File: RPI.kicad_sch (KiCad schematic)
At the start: 29 parts, among them J1 Conn_01x02_Male, J2 GPIO, J5 Conn_01x06, J6 Conn_01x04, J7 Conn_01x03, J8 Conn_01x02, J9 Conn_01x02, Q1 IRF9540N, Q2 IRF9540N, Q3 BC856BDW1, SW1 SW_SPDT, SW2 SW_SPDT, U1 LM1085-ADJ

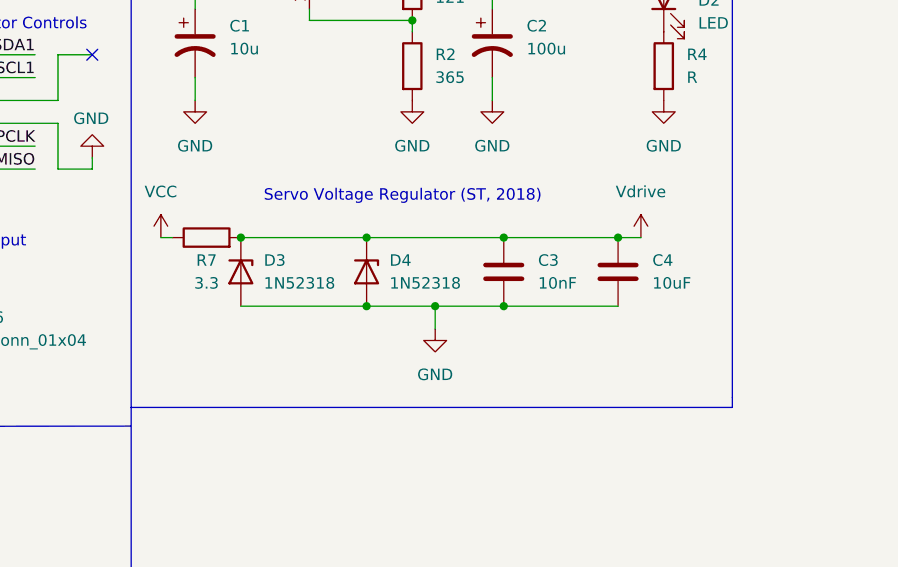
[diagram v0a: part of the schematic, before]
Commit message: Further updated with more resistors
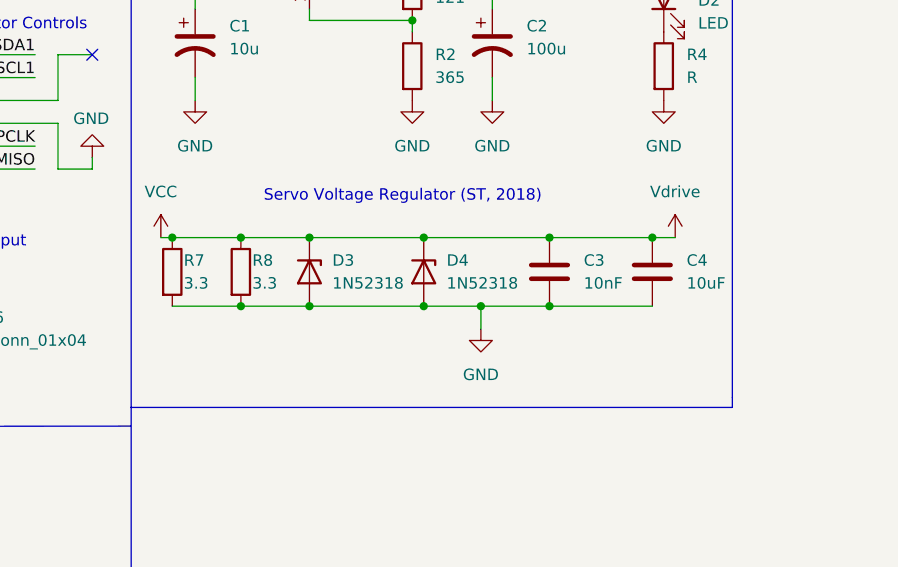
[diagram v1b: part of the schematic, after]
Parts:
- added R8: 3.3, Resistor_SMD:R_0805_2012Metric_Pad1.20x1.40mm_HandSolder, symbol Device:R
- R7: footprint Resistor_THT:R_Axial_DIN0207_L6.3mm_D2.5mm_P10.16mm_Horizontal -> Resistor_SMD:R_0805_2012Metric_Pad1.20x1.40mm_HandSolder
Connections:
- net GND: now also R7.2, R8.2
- net VCC: now also C3.1, C4.1, D3.1 (K), D4.1 (K), J7.2 (Pin_2), R8.1
- removed net Vdrive: C3.1, C4.1, D3.1 (K), D4.1 (K), J7.2 (Pin_2), R7.2
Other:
- moved on the sheet: C3, C4, D3, D4

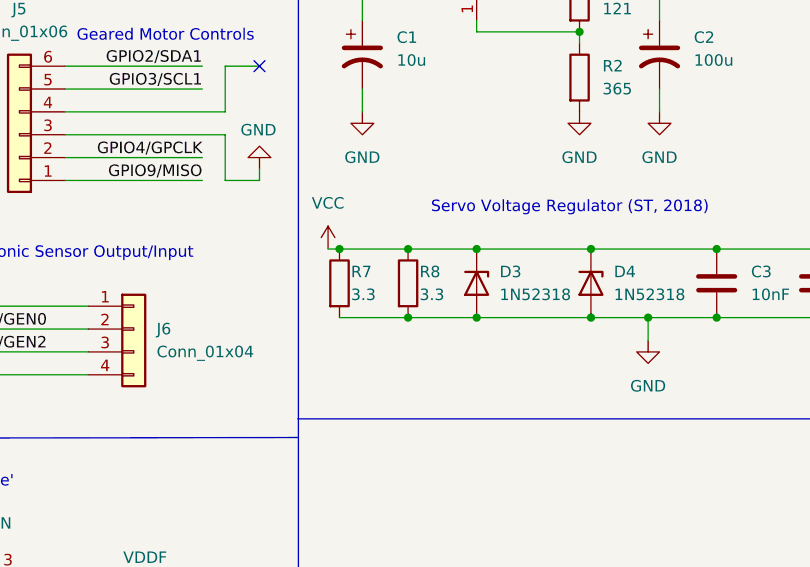
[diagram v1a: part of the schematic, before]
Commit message: Updated parallel res due to poor understanding
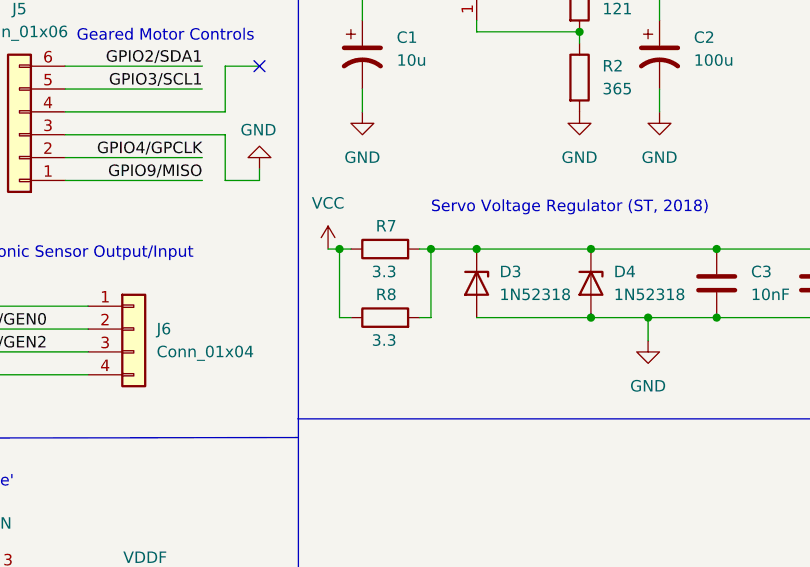
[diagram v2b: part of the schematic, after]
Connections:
- net GND: no longer R7.2, R8.2
- net VCC: no longer C3.1, C4.1, D3.1 (K), D4.1 (K), J7.2 (Pin_2)
- new net Vdrive: C3.1, C4.1, D3.1 (K), D4.1 (K), J7.2 (Pin_2), R7.2, R8.2
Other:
- moved on the sheet: R7, R8
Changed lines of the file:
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@@
     (date "15 nov 2012")
   )
+  (junction (at 109.22 118.11) (diameter 0) (color 0 0 0 0)
+  )
   (junction (at 127 40.64) (diameter 0) (color 0 0 0 0)
   )
@@
   (junction (at 121.92 125.73) (diameter 0) (color 0 0 0 0)
   )
+  (junction (at 93.98 118.11) (diameter 0) (color 0 0 0 0)
+  )
   (junction (at 148.59 85.09) (diameter 0) (color 0 0 0 0)
   )
@@
   (junction (at 36.83 74.93) (diameter 1.016) (color 0 0 0 0)
   )
-  (junction (at 93.98 118.11) (diameter 0) (color 0 0 0 0)
-  )
   (junction (at 36.83 57.15) (diameter 1.016) (color 0 0 0 0)
   )
   (junction (at 120.65 85.09) (diameter 0) (color 0 0 0 0)
   )
-  (junction (at 109.22 125.73) (diameter 0) (color 0 0 0 0)
-  )
   (junction (at 54.61 67.31) (diameter 1.016) (color 0 0 0 0)
   )
@@
   (junction (at 100.33 40.64) (diameter 0) (color 0 0 0 0)
   )
-  (junction (at 109.22 118.11) (diameter 0) (color 0 0 0 0)
-  )
   (junction (at 135.89 125.73) (diameter 0) (color 0 0 0 0)
   )
-  (junction (at 101.6 125.73) (diameter 0) (color 0 0 0 0)
-  )
   (junction (at 54.61 62.23) (diameter 1.016) (color 0 0 0 0)
   )
   (junction (at 44.45 173.99) (diameter 0) (color 0 0 0 0)
   )
-  (junction (at 101.6 118.11) (diameter 0) (color 0 0 0 0)
-  )
   (junction (at 129.54 85.09) (diameter 0) (color 0 0 0 0)
   )
   (junction (at 54.61 49.53) (diameter 1.016) (color 0 0 0 0)
+  )
+  (junction (at 104.14 118.11) (diameter 0) (color 0 0 0 0)
   )
   (junction (at 121.92 118.11) (diameter 0) (color 0 0 0 0)
@@
   (no_connect (at 137.16 36.83))
   (no_connect (at 137.16 49.53))
+  (wire (pts (xy 104.14 118.11) (xy 109.22 118.11))
+    (stroke (width 0) (type default) (color 0 0 0 0))
+  )
   (wire (pts (xy 36.83 57.15) (xy 36.83 74.93))
     (stroke (width 0) (type solid) (color 0 0 0 0))
@@
     (stroke (width 0) (type solid) (color 0 0 0 0))
   )
+  (wire (pts (xy 104.14 125.73) (xy 102.87 125.73))
+    (stroke (width 0) (type default) (color 0 0 0 0))
+  )
   (wire (pts (xy 54.61 49.53) (xy 52.07 49.53))
     (stroke (width 0) (type solid) (color 0 0 0 0))
@@
     (stroke (width 0) (type default) (color 0 0 0 0))
   )
-  (wire (pts (xy 93.98 118.11) (xy 101.6 118.11))
-    (stroke (width 0) (type default) (color 0 0 0 0))
-  )
   (wire (pts (xy 78.74 107.95) (xy 63.5 107.95))
     (stroke (width 0) (type default) (color 0 0 0 0))
@@
     (stroke (width 0) (type solid) (color 0 0 0 0))
   )
+  (wire (pts (xy 93.98 118.11) (xy 95.25 118.11))
+    (stroke (width 0) (type default) (color 0 0 0 0))
+  )
   (wire (pts (xy 96.52 85.09) (xy 96.52 92.71))
     (stroke (width 0) (type default) (color 0 0 0 0))
@@
     (stroke (width 0) (type default) (color 0 0 0 0))
   )
-  (wire (pts (xy 93.98 125.73) (xy 101.6 125.73))
-    (stroke (width 0) (type default) (color 0 0 0 0))
-  )
   (wire (pts (xy 20.32 97.79) (xy 34.29 97.79))
     (stroke (width 0) (type default) (color 0 0 0 0))
@@
     (stroke (width 0) (type solid) (color 0 0 0 0))
   )
+  (wire (pts (xy 93.98 118.11) (xy 93.98 125.73))
+    (stroke (width 0) (type default) (color 0 0 0 0))
+  )
   (wire (pts (xy 15.24 194.31) (xy 15.24 191.77))
     (stroke (width 0) (type default) (color 0 0 0 0))
@@
     (stroke (width 0) (type default) (color 0 0 0 0))
   )
-  (wire (pts (xy 101.6 125.73) (xy 109.22 125.73))
-    (stroke (width 0) (type default) (color 0 0 0 0))
-  )
   (wire (pts (xy 62.23 172.72) (xy 62.23 175.26))
     (stroke (width 0) (type default) (color 0 0 0 0))
@@
     (stroke (width 0) (type solid) (color 0 0 0 0))
   )
+  (wire (pts (xy 104.14 125.73) (xy 104.14 118.11))
+    (stroke (width 0) (type default) (color 0 0 0 0))
+  )
   (wire (pts (xy 49.53 127) (xy 66.04 127))
     (stroke (width 0) (type default) (color 0 0 0 0))
@@
     (stroke (width 0) (type solid) (color 0 0 0 0))
   )
+  (wire (pts (xy 93.98 125.73) (xy 95.25 125.73))
+    (stroke (width 0) (type default) (color 0 0 0 0))
+  )
   (wire (pts (xy 44.45 184.15) (xy 44.45 185.42))
     (stroke (width 0) (type default) (color 0 0 0 0))
@@
     (stroke (width 0) (type default) (color 0 0 0 0))
   )
-  (wire (pts (xy 101.6 118.11) (xy 109.22 118.11))
-    (stroke (width 0) (type default) (color 0 0 0 0))
-  )
   (wire (pts (xy 19.05 191.77) (xy 21.59 191.77))
     (stroke (width 0) (type default) (color 0 0 0 0))
@@
   )
   (wire (pts (xy 121.92 125.73) (xy 128.27 125.73))
+    (stroke (width 0) (type default) (color 0 0 0 0))
+  )
+  (wire (pts (xy 104.14 118.11) (xy 102.87 118.11))
     (stroke (width 0) (type default) (color 0 0 0 0))
   )
@@
     (pin "1")
   )
-  (symbol (lib_id "Device:R") (at 93.98 121.92 0) (unit 1)
-    (in_bom yes) (on_board yes)
-    (property "Reference" "R7" (id 0) (at 95.25 120.65 0)
-      (effects (font (size 1.27 1.27)) (justify left))
-    )
-    (property "Value" "3.3" (id 1) (at 95.25 123.19 0)
-      (effects (font (size 1.27 1.27)) (justify left))
-    )
-    (property "Footprint" "Resistor_SMD:R_0805_2012Metric_Pad1.20x1.40mm_HandSolder" (id 2) (at 92.202 121.92 90)
-      (effects (font (size 1.27 1.27)) hide)
-    )
-    (property "Datasheet" "~" (id 3) (at 93.98 121.92 0)
+  (symbol (lib_id "Device:R") (at 99.06 118.11 90) (unit 1)
+    (in_bom yes) (on_board yes)
+    (property "Reference" "R7" (id 0) (at 100.33 115.57 90)
+      (effects (font (size 1.27 1.27)) (justify left))
+    )
+    (property "Value" "3.3" (id 1) (at 100.33 120.65 90)
+      (effects (font (size 1.27 1.27)) (justify left))
+    )
+    (property "Footprint" "Resistor_SMD:R_0805_2012Metric_Pad1.20x1.40mm_HandSolder" (id 2) (at 99.06 119.888 90)
+      (effects (font (size 1.27 1.27)) hide)
+    )
+    (property "Datasheet" "~" (id 3) (at 99.06 118.11 0)
       (effects (font (size 1.27 1.27)) hide)
     )
@@
     (pin "1")
   )
-  (symbol (lib_id "Device:R") (at 101.6 121.92 0) (unit 1)
-    (in_bom yes) (on_board yes)
-    (property "Reference" "R8" (id 0) (at 102.87 120.65 0)
-      (effects (font (size 1.27 1.27)) (justify left))
-    )
-    (property "Value" "3.3" (id 1) (at 102.87 123.19 0)
-      (effects (font (size 1.27 1.27)) (justify left))
-    )
-    (property "Footprint" "Resistor_SMD:R_0805_2012Metric_Pad1.20x1.40mm_HandSolder" (id 2) (at 99.822 121.92 90)
-      (effects (font (size 1.27 1.27)) hide)
-    )
-    (property "Datasheet" "~" (id 3) (at 101.6 121.92 0)
-      (effects (font (size 1.27 1.27)) hide)
-    )
+  (symbol (lib_id "Device:R") (at 99.06 125.73 90) (unit 1)
+    (in_bom yes) (on_board yes)
+    (property "Reference" "R8" (id 0) (at 100.33 123.19 90)
+      (effects (font (size 1.27 1.27)) (justify left))
+    )
+    (property "Value" "3.3" (id 1) (at 100.33 128.27 90)
+      (effects (font (size 1.27 1.27)) (justify left))
+    )
+    (property "Footprint" "Resistor_SMD:R_0805_2012Metric_Pad1.20x1.40mm_HandSolder" (id 2) (at 99.06 127.508 90)
+      (effects (font (size 1.27 1.27)) hide)
+    )
+    (property "Datasheet" "~" (id 3) (at 99.06 125.73 0)
+      (effects (font (size 1.27 1.27)) hide)
+    )

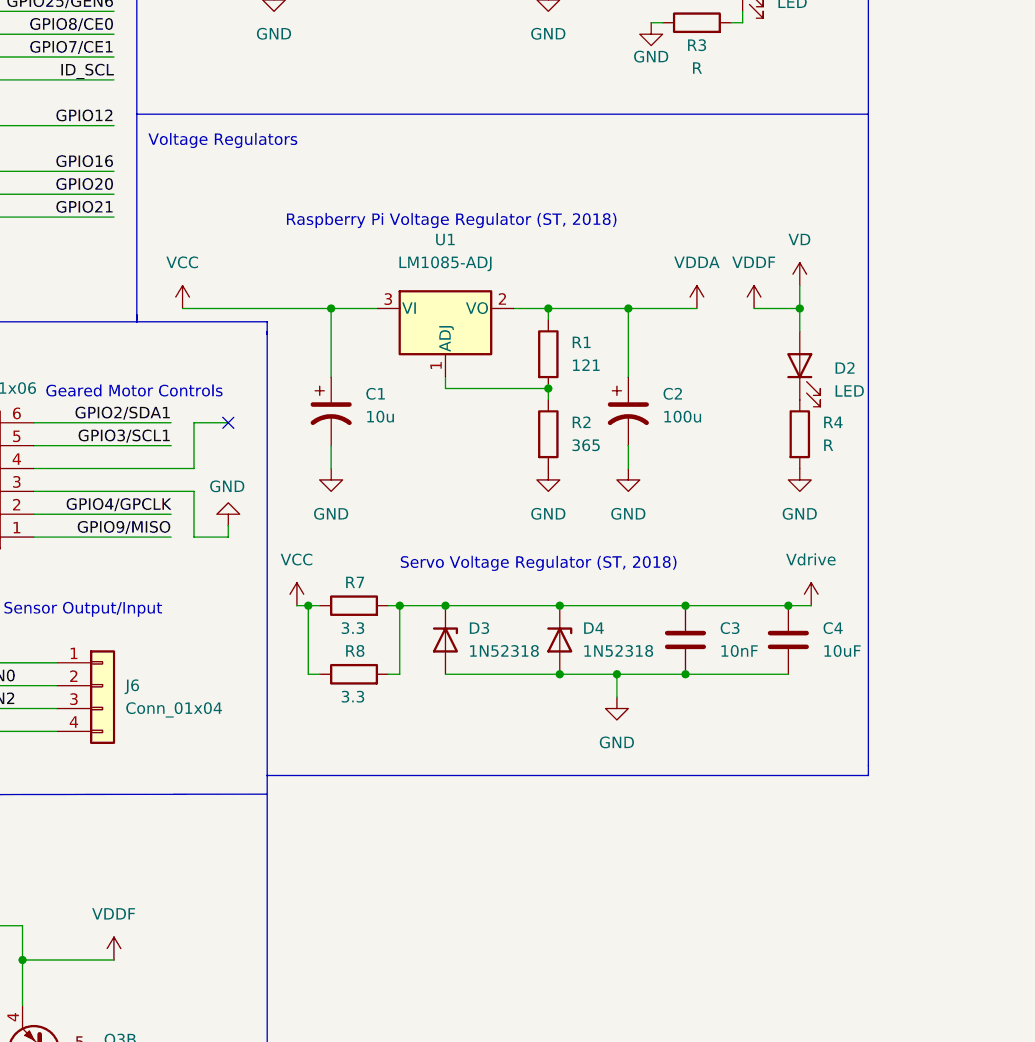
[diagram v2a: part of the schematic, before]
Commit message: Changed regulator
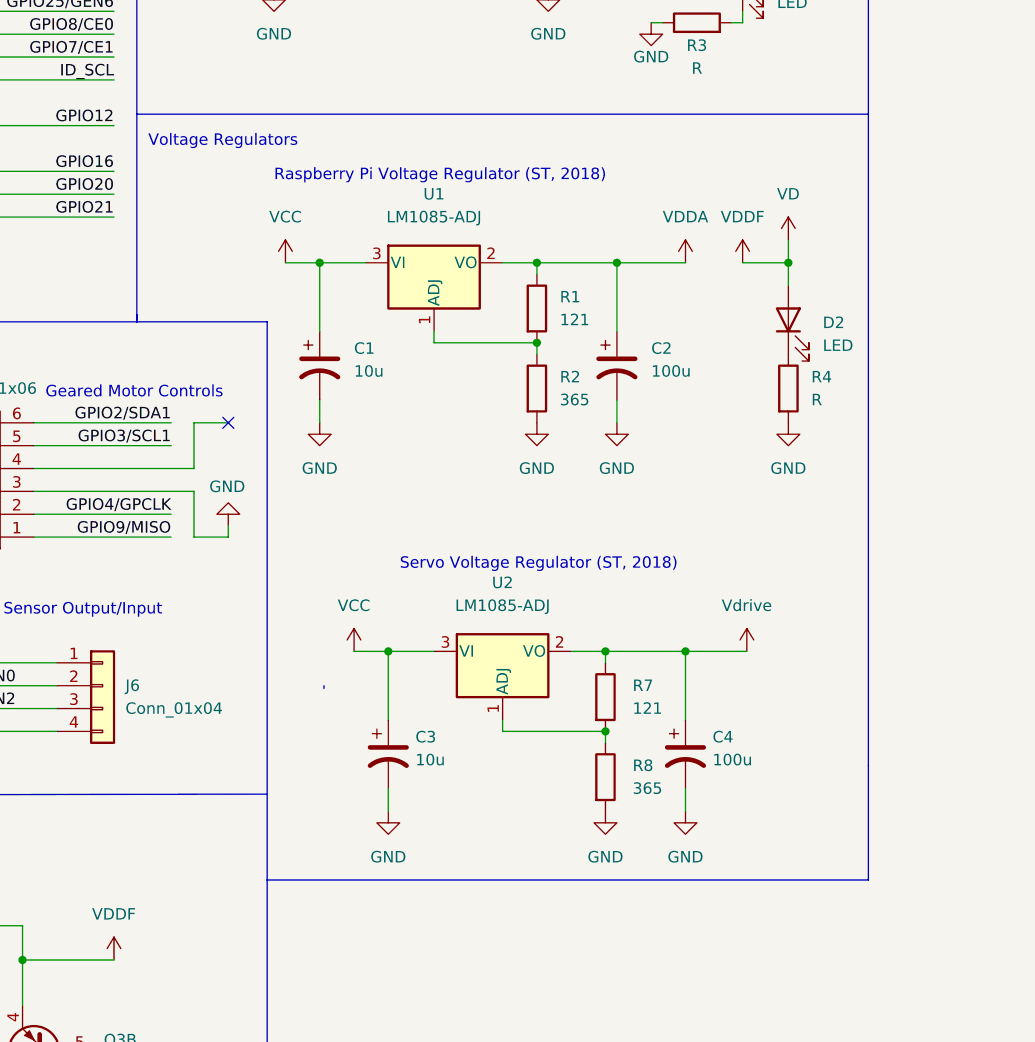
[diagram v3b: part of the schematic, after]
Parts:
- removed C3: 10nF, Capacitor_SMD:C_0805_2012Metric_Pad1.18x1.45mm_HandSolder, symbol Device:C
- removed C4: 10uF, Capacitor_SMD:C_0805_2012Metric_Pad1.18x1.45mm_HandSolder, symbol Device:C
- removed D3, D4: 1N52318, Diode_THT:D_DO-35_SOD27_P7.62mm_Horizontal, symbol Device:D_Zener
- added C3: 10u, Capacitor_THT:CP_Radial_D5.0mm_P2.50mm, symbol Device:C_Polarized_US
- added C4: 100u, Capacitor_Tantalum_SMD:CP_EIA-2012-12_Kemet-R_Pad1.30x1.05mm_HandSolder, symbol Device:C_Polarized_US
- added U2: LM1085-ADJ, RPi_Hat:LM1085-5.0, symbol Regulator_Linear:LM1085-ADJ
- R7: value 3.3 -> 121
- R8: value 3.3 -> 365
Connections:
- net GND: now also R8.2, C3.2, C4.2
- net VCC: now also C3.1, U2.3 (VI); no longer R7.1, R8.1
- net Vdrive: now also R7.1, C4.1, U2.2 (VO); no longer R7.2, R8.2
- new net: R7.2, R8.1, U2.1 (ADJ)
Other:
- moved on the sheet: C1, C2, D2, R1, R2, R4, U1
